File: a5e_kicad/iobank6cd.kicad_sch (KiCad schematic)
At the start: 1 part, among them U7 A5EB013B-B23B

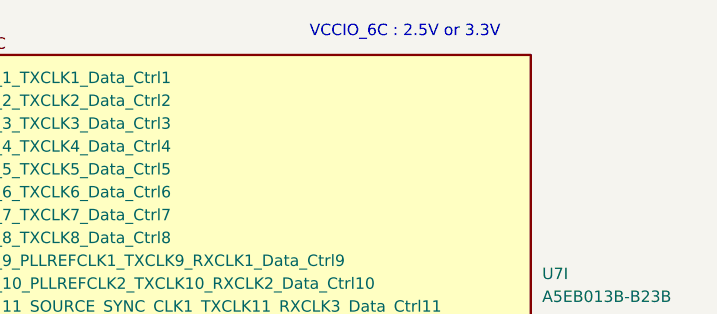
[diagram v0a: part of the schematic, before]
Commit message: Schematic reorg step 1: remove dangling stubs and stale notes, correct notes, fill title blocks
Netlist: 0 renamed, 0 connectivity diffs; DRC parity 0. ERC 315 -> 242.
Plan refreshed for the eMMC, RTL8211FDI, TPS548A28 and the tuned LPDDR4 (IOBANK 3 sheet name kept).
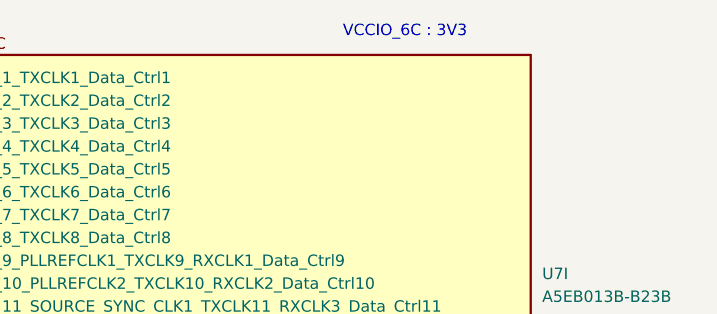
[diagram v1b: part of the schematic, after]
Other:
- note added: "VCCIO_6C : 3V3"
- note removed: "VCCIO_6C : 2.5V or 3.3V"
- company: Altera Germany GmbH -> (none)
- title: DBM_A5E013 -> Banks 6C / 6D HVIO
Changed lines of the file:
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@@
 	(paper "A4")
 	(title_block
-		(title "DBM_A5E013")
-		(rev "0.1")
-		(company "Altera Germany GmbH")
+		(title "Banks 6C / 6D HVIO")
+		(rev "${REVISION}")
+		(comment 1 "${BOARD}")
 	)
-	(text "VCCIO_6C : 2.5V or 3.3V"
+	(text "VCCIO_6C : 3V3"
 		(exclude_from_sim no)
 		(at 162.56 22.86 0)

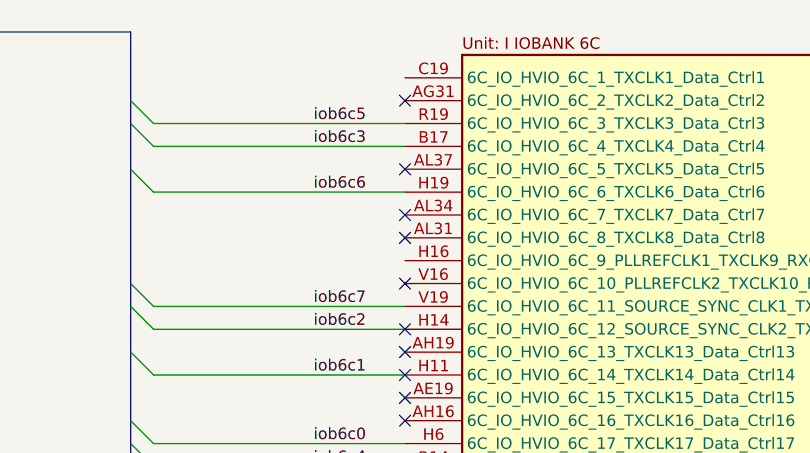
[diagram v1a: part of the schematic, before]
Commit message: Remove PHY swap leftovers R38/R29 (schematic and PCB), NC flags on bank 6C C19/H16
R38 1K0 had pin 1 alone on phy_led2, R29 4K7 pin 2 unconnected. Also removes the dead PHY LED2 labels,
bus entries and the orphan R29 pad-2 track. Netlist: only R29/R38 pins gone; DRC parity 0.
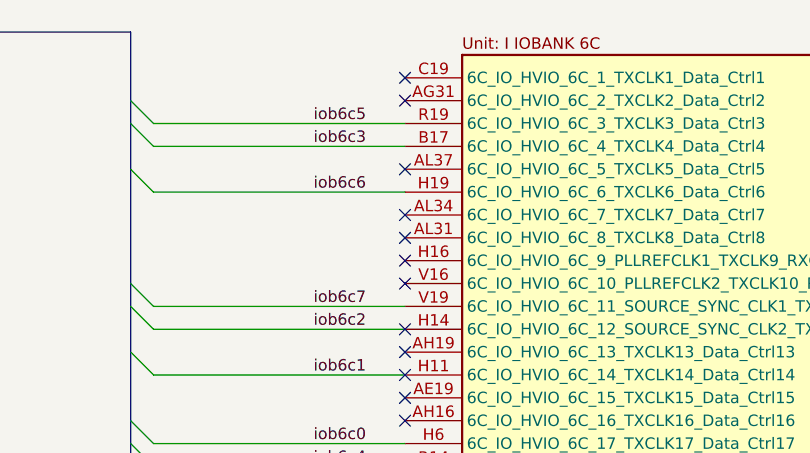
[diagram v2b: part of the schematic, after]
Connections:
- no-connect marks 12 -> 14
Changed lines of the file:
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@@
+	)
+	(no_connect
+		(at 96.52 27.94)
+	)
+	(no_connect
+		(at 96.52 48.26)
 	)
 	(no_connect

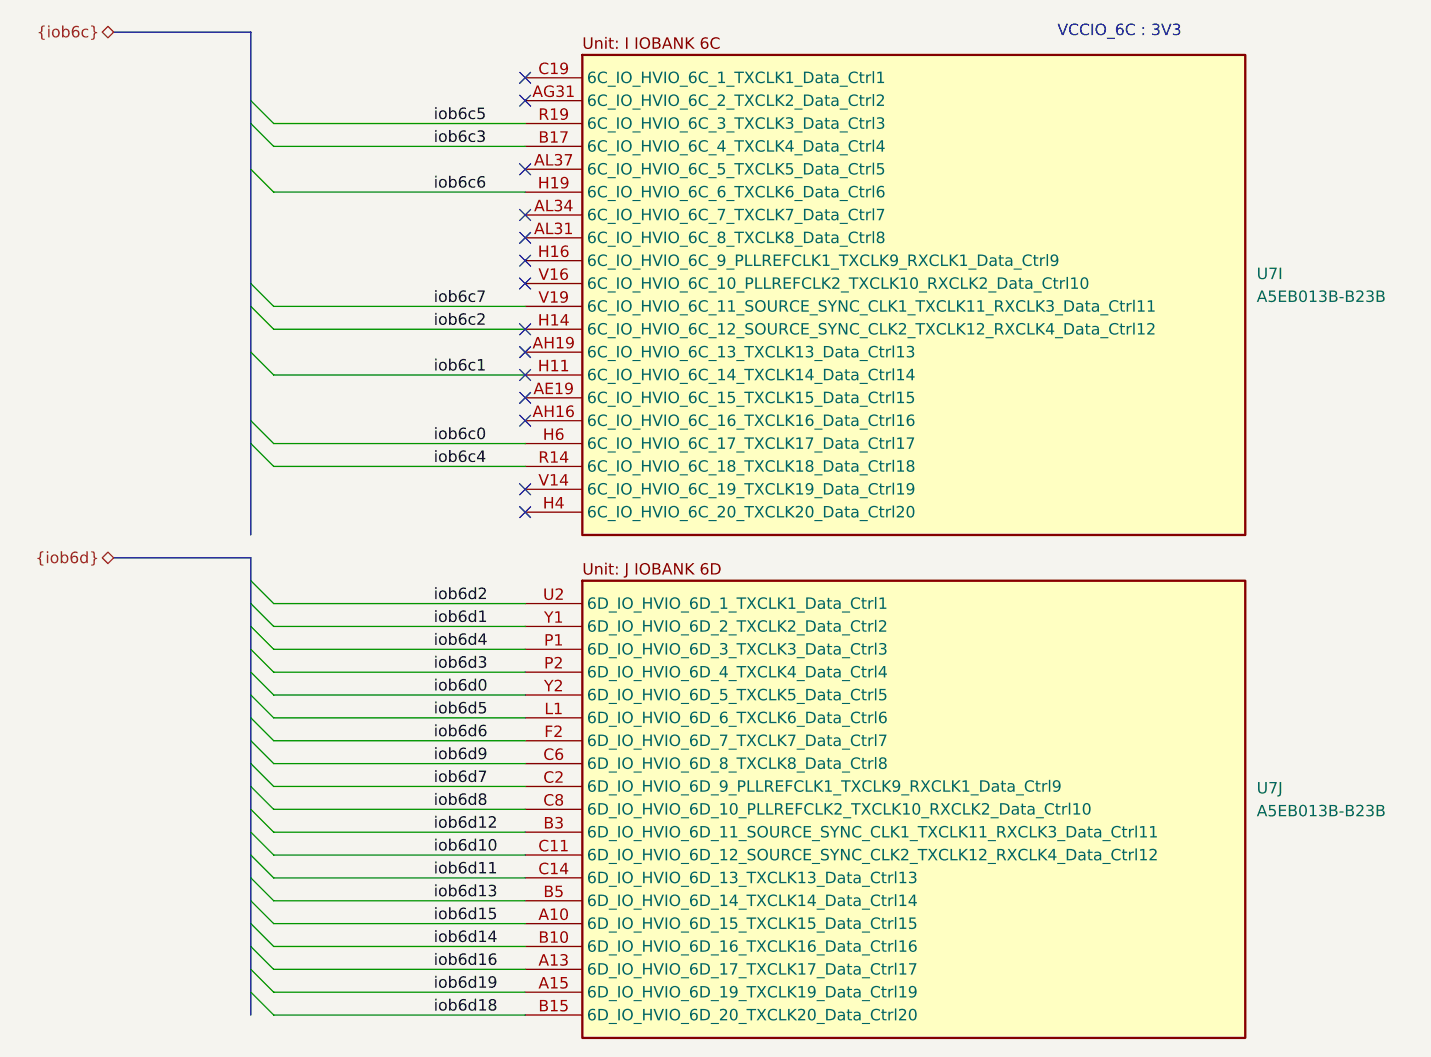
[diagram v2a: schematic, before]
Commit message: Schematic reorg step 7: no global labels, NC flags on unused U7 pins
- hps_uart0_tx/rx, eth_rst_n, phy_rst_n, fpga_led: global labels replaced by
  sheet pins; eth_led_g_n is a local label
- HyperBus labels/bus, the HPS {hps_i2c} bus and the pwr_scl/pwr_sda wiring
  removed (nothing behind them)
- 118 U7 pins that only had a net label: label, stub and bus entry removed,
  no-connect flag added
- Bank 3A notes restacked
- PCB: 124 nets renamed (118 to unconnected-(U7...))

Netdiff: 124 renamed, 0 connectivity diffs. ERC 148 -> 21. DRC parity 0.
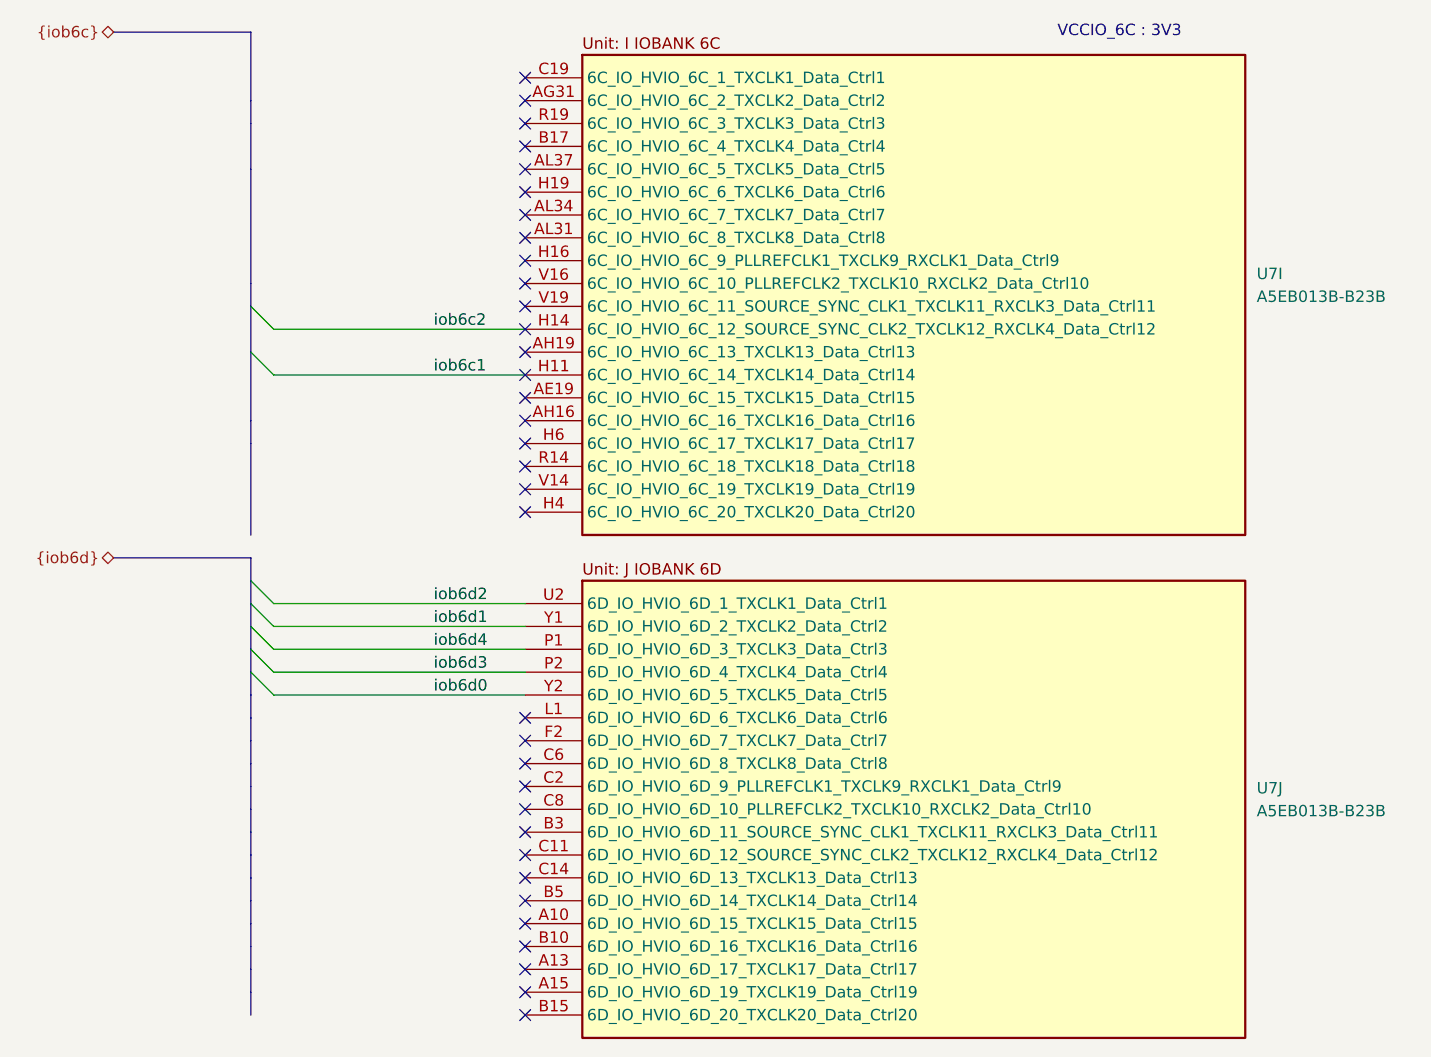
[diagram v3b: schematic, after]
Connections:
- net iob6c0: no longer names the net of U7.H6 (6C_IO_HVIO_6C_17_TXCLK17_Data_Ctrl17)
- net iob6c3: no longer names the net of U7.B17 (6C_IO_HVIO_6C_4_TXCLK4_Data_Ctrl4)
- net iob6c4: no longer names the net of U7.R14 (6C_IO_HVIO_6C_18_TXCLK18_Data_Ctrl18)
- net iob6c5: no longer names the net of U7.R19 (6C_IO_HVIO_6C_3_TXCLK3_Data_Ctrl3)
- net iob6c6: no longer names the net of U7.H19 (6C_IO_HVIO_6C_6_TXCLK6_Data_Ctrl6)
- net iob6c7: no longer names the net of U7.V19 (6C_IO_HVIO_6C_11_SOURCE_SYNC_CLK1_TXCLK11_RXCLK3_Data_Ctrl11)
- net iob6d10: no longer names the net of U7.C11 (6D_IO_HVIO_6D_12_SOURCE_SYNC_CLK2_TXCLK12_RXCLK4_Data_Ctrl12)
- net iob6d11: no longer names the net of U7.C14 (6D_IO_HVIO_6D_13_TXCLK13_Data_Ctrl13)
- net iob6d12: no longer names the net of U7.B3 (6D_IO_HVIO_6D_11_SOURCE_SYNC_CLK1_TXCLK11_RXCLK3_Data_Ctrl11)
- net iob6d13: no longer names the net of U7.B5 (6D_IO_HVIO_6D_14_TXCLK14_Data_Ctrl14)
- net iob6d14: no longer names the net of U7.B10 (6D_IO_HVIO_6D_16_TXCLK16_Data_Ctrl16)
- net iob6d15: no longer names the net of U7.A10 (6D_IO_HVIO_6D_15_TXCLK15_Data_Ctrl15)
- net iob6d16: no longer names the net of U7.A13 (6D_IO_HVIO_6D_17_TXCLK17_Data_Ctrl17)
- net iob6d18: no longer names the net of U7.B15 (6D_IO_HVIO_6D_20_TXCLK20_Data_Ctrl20)
- net iob6d19: no longer names the net of U7.A15 (6D_IO_HVIO_6D_19_TXCLK19_Data_Ctrl19)
- net iob6d5: no longer names the net of U7.L1 (6D_IO_HVIO_6D_6_TXCLK6_Data_Ctrl6)
- net iob6d6: no longer names the net of U7.F2 (6D_IO_HVIO_6D_7_TXCLK7_Data_Ctrl7)
- net iob6d7: no longer names the net of U7.C2 (6D_IO_HVIO_6D_9_PLLREFCLK1_TXCLK9_RXCLK1_Data_Ctrl9)
- net iob6d8: no longer names the net of U7.C8 (6D_IO_HVIO_6D_10_PLLREFCLK2_TXCLK10_RXCLK2_Data_Ctrl10)
- net iob6d9: no longer names the net of U7.C6 (6D_IO_HVIO_6D_8_TXCLK8_Data_Ctrl8)
- no-connect marks 14 -> 34
